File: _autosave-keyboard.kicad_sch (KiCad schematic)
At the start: 25 parts, among them SW1 SW_Push, SW10 SW_Push, SW11 SW_Push, SW12 RotaryEncoder_Switch, SW2 SW_Push, SW3 SW_Push, SW4 SW_Push, SW5 SW_Push, SW6 SW_Push, SW7 SW_Push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

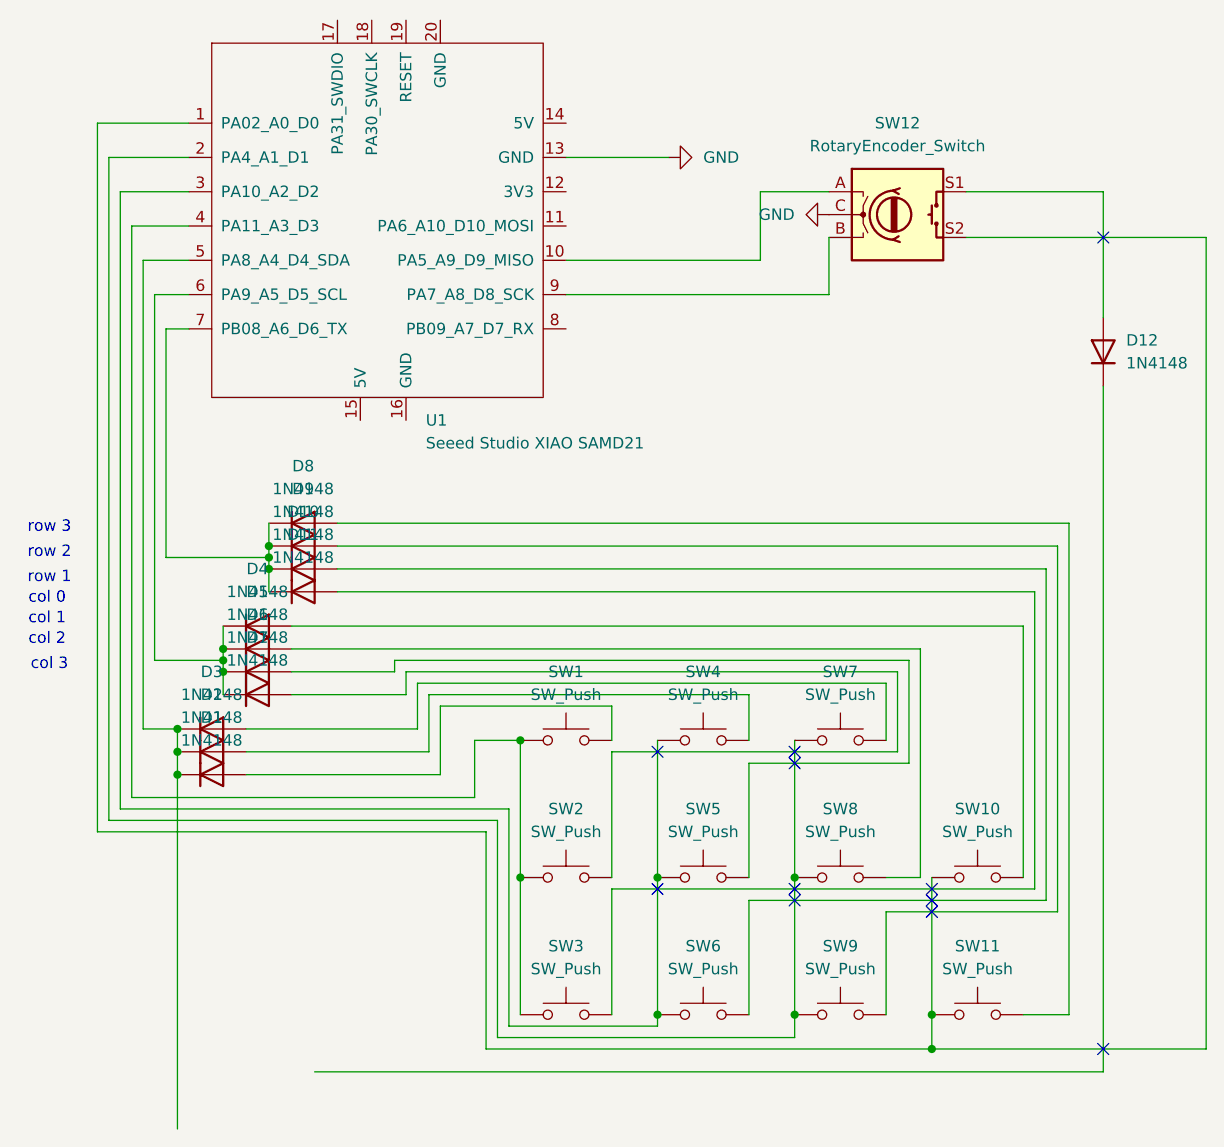
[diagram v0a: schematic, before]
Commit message: rewired the rotary encoder into the matrix
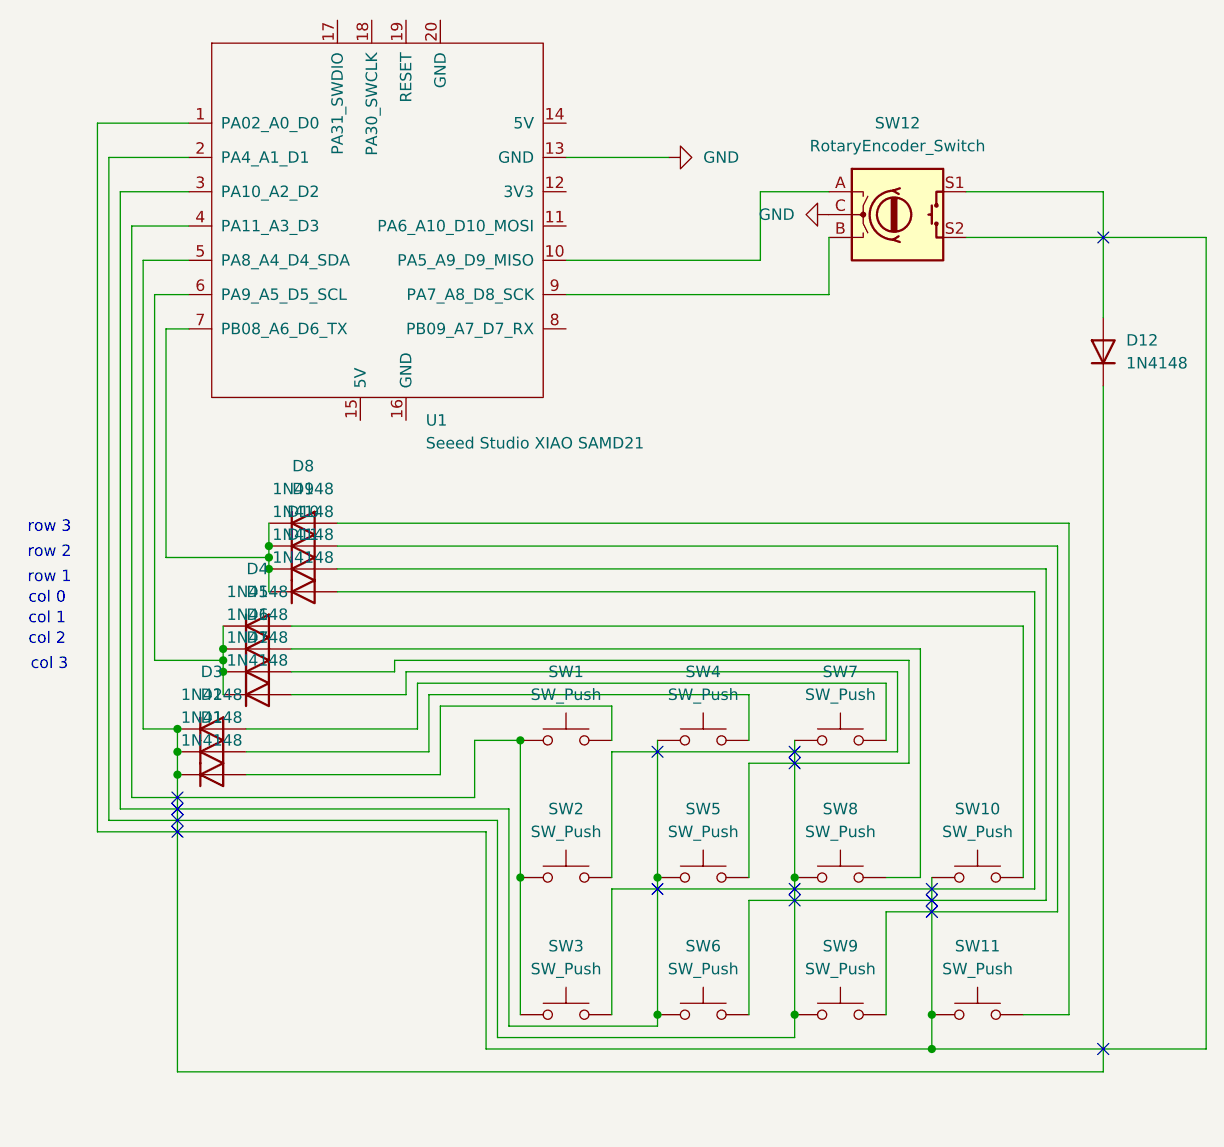
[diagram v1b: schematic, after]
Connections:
- net at D12.1 (K): now also D1.1 (K), D2.1 (K), D3.1 (K), U1.5 (PA8_A4_D4_SDA)
- no-connect marks 11 -> 15
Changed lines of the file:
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@@
+	)
+	(no_connect
+		(at 114.3 129.54)
 	)
 	(no_connect
@@
 	)
 	(no_connect
+		(at 114.3 132.08)
+	)
+	(no_connect
 		(at 198.12 139.7)
 	)
@@
 	)
 	(no_connect
+		(at 114.3 130.81)
+	)
+	(no_connect
+		(at 114.3 133.35)
+	)
+	(no_connect
 		(at 167.64 124.46)
 	)
@@
 	(wire
 		(pts
+			(xy 114.3 160.02) (xy 217.17 160.02)
+		)
+		(stroke
+			(width 0)
+			(type default)
+		)
+	)
+	(wire
+		(pts
 			(xy 208.28 153.67) (xy 213.36 153.67)
 		)
@@
 	(wire
 		(pts
-			(xy 129.54 160.02) (xy 217.17 160.02)
-		)
-		(stroke
-			(width 0)
-			(type default)
-		)
-	)
-	(wire
-		(pts
 			(xy 119.38 115.57) (xy 119.38 118.11)
 		)
@@
 	(wire
 		(pts
-			(xy 114.3 127) (xy 114.3 166.37)
-		)
-		(stroke
+			(xy 114.3 127) (xy 114.3 160.02)
+		)
+		(stroke
